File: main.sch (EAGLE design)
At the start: 45 parts, among them IC10 FGPMMOPA6H, IC2 25LC1024-I/P, IC6 MPL3115A2LGA, IC7 FXAS21000, IC8 ADXL343BCCZ, Q1 12MHz, U1 ATMEGA1284P-PU, U2 LTC3440EMSPBF

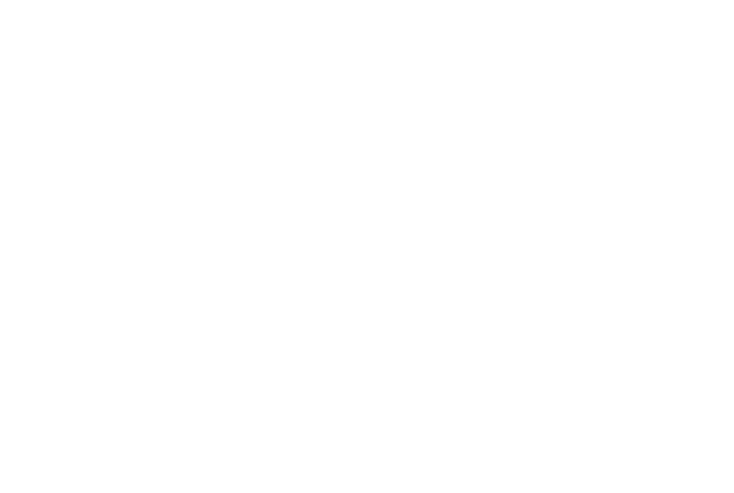
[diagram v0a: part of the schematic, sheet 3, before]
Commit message: Added datasheet for MCP9700A temperature sensor and added ambient temperature sensor to schematic.
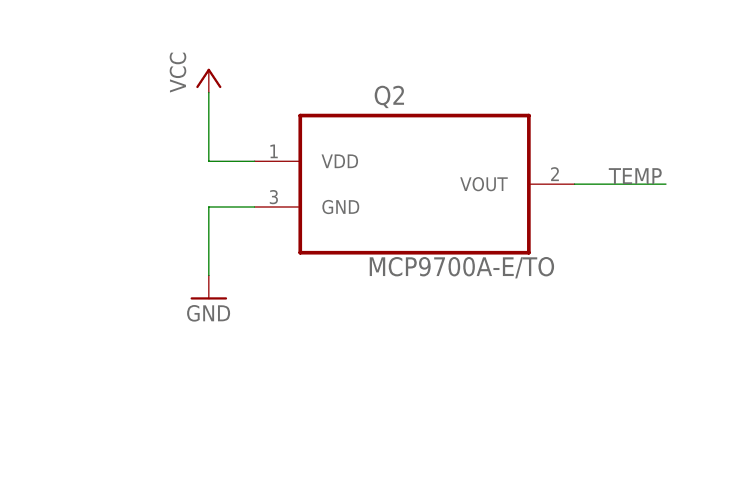
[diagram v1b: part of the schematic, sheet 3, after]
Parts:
- added Q2: MCP9700A-E/TO, CU in Space:MCP9700A-E/TO
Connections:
- removed net U2_TRIGGER: U1.PB0
- new net TEMP: Q2.VOUT, U1.PA0
- net GND: now also Q2.GND
- net VCC: now also Q2.VDD
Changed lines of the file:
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@@
 <part name="C10" library="rcl" library_urn="urn:adsk.eagle:library:334" deviceset="C-EU" device="025-025X050" package3d_urn="urn:adsk.eagle:package:23629/2" value="47pF"/>
 <part name="C11" library="rcl" library_urn="urn:adsk.eagle:library:334" deviceset="C-EU" device="025-025X050" package3d_urn="urn:adsk.eagle:package:23629/2" value="1µF"/>
+<part name="Q2" library="CU in Space" deviceset="MCP9700A-E/TO" device=""/>
+<part name="P+6" library="supply1" library_urn="urn:adsk.eagle:library:371" deviceset="VCC" device=""/>
+<part name="GND7" library="supply1" library_urn="urn:adsk.eagle:library:371" deviceset="GND" device=""/>
 </parts>
 <sheets>
@@
 </segment>
 </net>
-<net name="U2_TRIGGER" class="0">
-<segment>
-<pinref part="U1" gate="A" pin="PB0"/>
-<wire x1="45.72" y1="116.84" x2="27.94" y2="116.84" width="0.1524" layer="91"/>
-<label x="27.94" y="116.84" size="1.778" layer="95"/>
-</segment>
-</net>
 <net name="U2_RESET" class="0">
 <segment>
@@
 <wire x1="45.72" y1="111.76" x2="27.94" y2="111.76" width="0.1524" layer="91"/>
 <label x="27.94" y="111.76" size="1.778" layer="95"/>
+</segment>
+</net>
+<net name="TEMP" class="0">
+<segment>
+<pinref part="U1" gate="A" pin="PA0"/>
+<wire x1="45.72" y1="139.7" x2="38.1" y2="139.7" width="0.1524" layer="91"/>
+<label x="38.1" y="139.7" size="1.778" layer="95"/>
 </segment>
 </net>
@@
 <instance part="FRAME1" gate="G$1" x="0" y="0"/>
 <instance part="FRAME1" gate="G$2" x="147.32" y="0"/>
+<instance part="Q2" gate="A" x="210.82" y="162.56"/>
+<instance part="P+6" gate="VCC" x="187.96" y="172.72"/>
+<instance part="GND7" gate="1" x="187.96" y="147.32"/>
 </instances>
 <busses>
@@
 <junction x="78.74" y="43.18"/>
 </segment>
+<segment>
+<pinref part="Q2" gate="A" pin="GND"/>
+<pinref part="GND7" gate="1" pin="GND"/>
+<wire x1="193.04" y1="157.48" x2="187.96" y2="157.48" width="0.1524" layer="91"/>
+<wire x1="187.96" y1="157.48" x2="187.96" y2="149.86" width="0.1524" layer="91"/>
+</segment>
 </net>
 <net name="VCC" class="0">
@@
 <junction x="27.94" y="76.2"/>
 </segment>
+<segment>
+<pinref part="Q2" gate="A" pin="VDD"/>
+<pinref part="P+6" gate="VCC" pin="VCC"/>
+<wire x1="193.04" y1="162.56" x2="187.96" y2="162.56" width="0.1524" layer="91"/>
+<wire x1="187.96" y1="162.56" x2="187.96" y2="170.18" width="0.1524" layer="91"/>
+</segment>
 </net>
 <net name="SCL" class="0">
@@
 </segment>
 </net>
+<net name="TEMP" class="0">
+<segment>
+<pinref part="Q2" gate="A" pin="VOUT"/>
+<wire x1="228.6" y1="160.02" x2="238.76" y2="160.02" width="0.1524" layer="91"/>
+<label x="232.41" y="160.02" size="1.778" layer="95"/>
+</segment>
+</net>

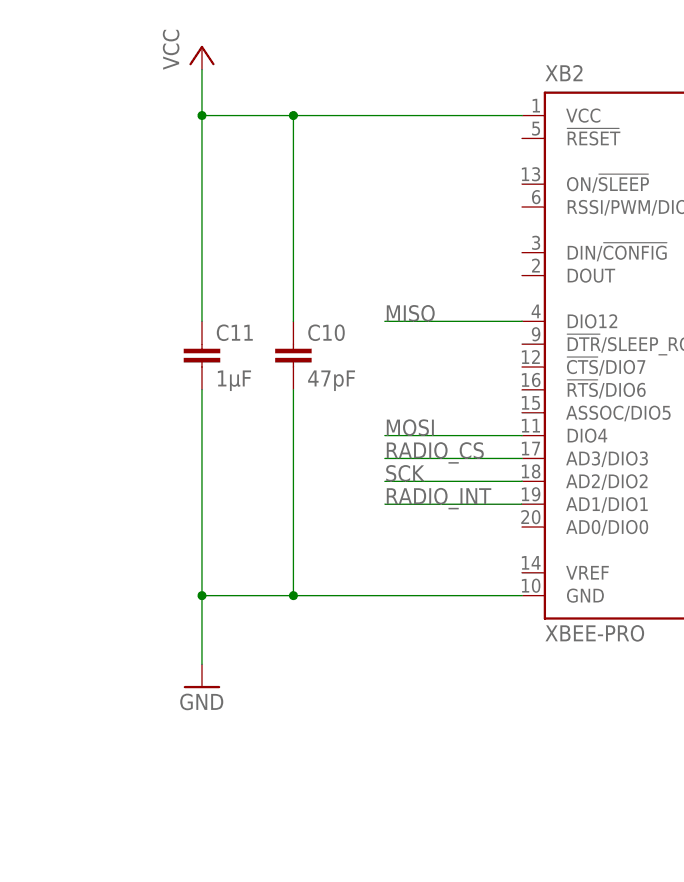
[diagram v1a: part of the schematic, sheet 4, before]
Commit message: Added high value pullups to SPI CS pins to avoid problems during programming
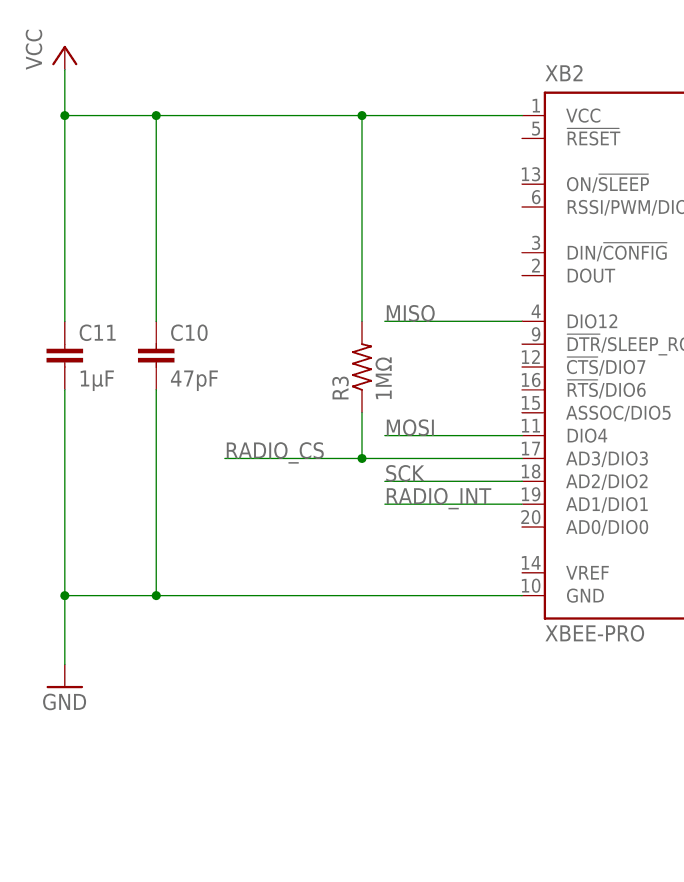
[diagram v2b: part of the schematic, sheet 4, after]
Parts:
- added R2, R3: 1MΩ, rcl:R-US_0207/5V
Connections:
- net EEPROM_CS: now also R2.1
- net RADIO_CS: now also R3.1
- net VCC: now also R2.2, R3.2
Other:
- moved on the sheet: C10, C11
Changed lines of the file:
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@@
 <part name="P+6" library="supply1" library_urn="urn:adsk.eagle:library:371" deviceset="VCC" device=""/>
 <part name="GND7" library="supply1" library_urn="urn:adsk.eagle:library:371" deviceset="GND" device=""/>
+<part name="P+7" library="supply1" library_urn="urn:adsk.eagle:library:371" deviceset="VCC" device=""/>
+<part name="R2" library="rcl" library_urn="urn:adsk.eagle:library:334" deviceset="R-US_" device="0207/5V" package3d_urn="urn:adsk.eagle:package:23502/1" value="1MΩ"/>
+<part name="R3" library="rcl" library_urn="urn:adsk.eagle:library:334" deviceset="R-US_" device="0207/5V" package3d_urn="urn:adsk.eagle:package:23502/1" value="1MΩ"/>
 </parts>
 <sheets>
@@
 <instance part="FRAME3" gate="G$1" x="0" y="-2.54"/>
 <instance part="FRAME3" gate="G$2" x="147.32" y="-2.54"/>
+<instance part="P+7" gate="VCC" x="180.34" y="129.54"/>
+<instance part="R2" gate="G$1" x="180.34" y="119.38" rot="R90"/>
 </instances>
 <busses>
@@
 <wire x1="147.32" y1="172.72" x2="147.32" y2="170.18" width="0.1524" layer="91"/>
 </segment>
+<segment>
+<pinref part="P+7" gate="VCC" pin="VCC"/>
+<pinref part="R2" gate="G$1" pin="2"/>
+<wire x1="180.34" y1="127" x2="180.34" y2="124.46" width="0.1524" layer="91"/>
+</segment>
 </net>
 <net name="XTAL1" class="0">
@@
 <segment>
 <pinref part="IC2" gate="G$1" pin="!CS"/>
-<wire x1="187.96" y1="111.76" x2="167.64" y2="111.76" width="0.1524" layer="91"/>
-<label x="167.64" y="111.76" size="1.778" layer="95"/>
+<wire x1="187.96" y1="111.76" x2="180.34" y2="111.76" width="0.1524" layer="91"/>
+<label x="162.56" y="111.76" size="1.778" layer="95"/>
+<pinref part="R2" gate="G$1" pin="1"/>
+<wire x1="180.34" y1="111.76" x2="162.56" y2="111.76" width="0.1524" layer="91"/>
+<wire x1="180.34" y1="114.3" x2="180.34" y2="111.76" width="0.1524" layer="91"/>
+<junction x="180.34" y="111.76"/>
 </segment>
 </net>
@@
 <instance part="FRAME4" gate="G$2" x="147.32" y="0"/>
 <instance part="XB2" gate="G$1" x="101.6" y="121.92"/>
-<instance part="P+5" gate="VCC" x="50.8" y="154.94"/>
-<instance part="GND6" gate="1" x="50.8" y="83.82"/>
-<instance part="C10" gate="G$1" x="60.96" y="121.92"/>
-<instance part="C11" gate="G$1" x="50.8" y="121.92"/>
+<instance part="P+5" gate="VCC" x="35.56" y="154.94"/>
+<instance part="GND6" gate="1" x="35.56" y="83.82"/>
+<instance part="C10" gate="G$1" x="45.72" y="121.92"/>
+<instance part="C11" gate="G$1" x="35.56" y="121.92"/>
+<instance part="R3" gate="G$1" x="68.58" y="119.38" rot="R90"/>
 </instances>
 <busses>
@@
 <segment>
 <pinref part="GND6" gate="1" pin="GND"/>
-<wire x1="50.8" y1="116.84" x2="50.8" y2="93.98" width="0.1524" layer="91"/>
+<wire x1="35.56" y1="116.84" x2="35.56" y2="93.98" width="0.1524" layer="91"/>
 <pinref part="XB2" gate="G$1" pin="GND"/>
-<wire x1="50.8" y1="93.98" x2="50.8" y2="86.36" width="0.1524" layer="91"/>
-<wire x1="86.36" y1="93.98" x2="60.96" y2="93.98" width="0.1524" layer="91"/>
-<junction x="50.8" y="93.98"/>
+<wire x1="35.56" y1="93.98" x2="35.56" y2="86.36" width="0.1524" layer="91"/>
+<wire x1="86.36" y1="93.98" x2="45.72" y2="93.98" width="0.1524" layer="91"/>
+<junction x="35.56" y="93.98"/>
 <pinref part="C10" gate="G$1" pin="2"/>
-<wire x1="60.96" y1="93.98" x2="50.8" y2="93.98" width="0.1524" layer="91"/>
-<wire x1="60.96" y1="116.84" x2="60.96" y2="93.98" width="0.1524" layer="91"/>
-<junction x="60.96" y="93.98"/>
+<wire x1="45.72" y1="93.98" x2="35.56" y2="93.98" width="0.1524" layer="91"/>
+<wire x1="45.72" y1="116.84" x2="45.72" y2="93.98" width="0.1524" layer="91"/>
+<junction x="45.72" y="93.98"/>
 <pinref part="C11" gate="G$1" pin="2"/>
 </segment>
@@
 <pinref part="XB2" gate="G$1" pin="VCC"/>
 <pinref part="P+5" gate="VCC" pin="VCC"/>
-<wire x1="86.36" y1="147.32" x2="60.96" y2="147.32" width="0.1524" layer="91"/>
-<wire x1="60.96" y1="147.32" x2="50.8" y2="147.32" width="0.1524" layer="91"/>
-<wire x1="50.8" y1="147.32" x2="50.8" y2="152.4" width="0.1524" layer="91"/>
-<wire x1="50.8" y1="147.32" x2="50.8" y2="124.46" width="0.1524" layer="91"/>
-<junction x="50.8" y="147.32"/>
+<wire x1="86.36" y1="147.32" x2="68.58" y2="147.32" width="0.1524" layer="91"/>
+<wire x1="68.58" y1="147.32" x2="45.72" y2="147.32" width="0.1524" layer="91"/>
+<wire x1="45.72" y1="147.32" x2="35.56" y2="147.32" width="0.1524" layer="91"/>
+<wire x1="35.56" y1="147.32" x2="35.56" y2="152.4" width="0.1524" layer="91"/>
+<wire x1="35.56" y1="147.32" x2="35.56" y2="124.46" width="0.1524" layer="91"/>
+<junction x="35.56" y="147.32"/>
 <pinref part="C10" gate="G$1" pin="1"/>
-<wire x1="60.96" y1="147.32" x2="60.96" y2="124.46" width="0.1524" layer="91"/>
-<junction x="60.96" y="147.32"/>
+<wire x1="45.72" y1="147.32" x2="45.72" y2="124.46" width="0.1524" layer="91"/>
+<junction x="45.72" y="147.32"/>
 <pinref part="C11" gate="G$1" pin="1"/>
+<pinref part="R3" gate="G$1" pin="2"/>
+<wire x1="68.58" y1="124.46" x2="68.58" y2="147.32" width="0.1524" layer="91"/>
+<junction x="68.58" y="147.32"/>
 </segment>
 </net>
@@
 <segment>
 <pinref part="XB2" gate="G$1" pin="AD3/DIO3"/>
-<wire x1="86.36" y1="109.22" x2="71.12" y2="109.22" width="0.1524" layer="91"/>
-<label x="71.12" y="109.22" size="1.778" layer="95"/>
-</segment>
-</net>
+<wire x1="86.36" y1="109.22" x2="68.58" y2="109.22" width="0.1524" layer="91"/>
+<label x="53.34" y="109.22" size="1.778" layer="95"/>
+<pinref part="R3" gate="G$1" pin="1"/>
+<wire x1="68.58" y1="109.22" x2="53.34" y2="109.22" width="0.1524" layer="91"/>
+<wire x1="68.58" y1="114.3" x2="68.58" y2="109.22" width="0.1524" layer="91"/>
+<junction x="68.58" y="109.22"/>
+</segment>
+</net>

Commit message: Voltage Regulator added
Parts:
- removed BAT1: (no value), adafruit:JST_2PIN-THM
- removed C24: 22µF, rcl:CPOL-USE2-5
- removed C25: 1.5nF, rcl:C-EU025-025X050
- removed RT1: 60.4kΩ, rcl:R-US_0207/5V
- added C12, C15: 1n, Power:K102K15X7RF5TL2
- added C13, C14: 22u, Power:UST1V220MDD
- added C16: 10n, Power:K103K15X7RF5TL2
- added C18: (no value), Power:K104K15X7RF5TL2
- added C19: (no value), Power:UST1V220MDD
- added C20: (no value), Power:FG18X7R1A225KRT06
- added D1, D2, D3: (no value), Power:SB230TA
- added L1: 18u, Power:RLB0914-180KL
- added R11: 24.9k, Power:MFR-25FBF52-24K9
- added R12: 51.1k, Power:MFR-25FBF52-51K1
- added R13: 17.4k, Power:MFR-25FBF52-17K4
- added R14: (no value), Power:MFR-25FBF52-51K1
- added R15: (no value), Power:MFR-25FBF52-26K7
- added R7: 8.06k, Power:MFR-25FBF52-8K06
- added U3: 2N3904BU, Power:2N3904BU
- C7: value 10µF -> 10n; device rcl:CPOL-USE2-5 -> Power:K103K15X7RF5TL2
- L3: value 10µH -> (none); device rcl:L-US0207/5V -> Power:B78108E1472K000
- R10: value 15kΩ -> 24.9k; device rcl:R-US_0207/5V -> Power:MFR-25FBF52-24K9
- R8: value 340kΩ -> 51.1k; device rcl:R-US_0207/5V -> Power:MFR-25FBF52-51K1
- R9: value 200kΩ -> 3.65k; device rcl:R-US_0207/5V -> Power:MFR-25FBF52-3K65
- U2: value LTC3440EMSPBF -> LT3570EFEPBF; device CU in Space:LTC3440EMSPBF -> Power:LT3570EFEPBF
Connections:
- removed net FB: R10.1, R8.1, R9.2, U2.FB
- removed net N$14: C25.1, U2.VC
- removed net VBAT1: BAT1.2, C7.+, U2.VIN, U2.~SHDN/SS
- new net +12.0: C14.+, D1.C, R8.11
- new net +2.5: C20.1, R14.11, U3.E
- new net FB1: R8.22, R9.11, U2.FB1
- new net N$15: R12.11, R13.22, U2.FB2
- new net N$16: C18.1, D3.C, U2.BOOST
- new net N$17: R14.22, R15.11, U2.FB3
- new net N$5: C7.1, U2.SS2
- new net N$6: R7.22, U2.RT
- new net N$7: R10.22, U2.VC2
- new net N$8: D1.A, L1.2, U2.SW1
- new net N$9: C15.1, R11.22
- new net NPN_DRV: U2.NPN_DRV, U3.B
- new net PWR_JUNC: C13.+, L1.1, U2.!SHDN1, U2.!SHDN2, U2.!SHDN3, U2.VIN1, U2.VIN2, U2.VIN3
- net GND: now also C12.2, C13.-, C14.-, C15.2, C16.2, C19.-, C20.2, C7.2, D2.A, R13.11, R15.22, R7.11, R9.22, U2.GND, U2.SYNC; no longer BAT1.1, C24.-, C7.-, R9.1, RT1.1, U2.MODE/SYNC
- net N$10: now also C12.1, R10.11; no longer L3.1, U2.SW1
- net N$11: now also R11.11, U2.VC1; no longer L3.2, U2.SW2
- net N$12: now also C16.1, U2.SS1; no longer RT1.2, U2.RT
- net N$13: now also C18.2, D2.C, L3.1, U2.SW2; no longer C25.2, R10.2
- net VCC: now also C19.+, D3.A, L3.2, R12.22, U3.C; no longer C24.+, R8.2, U2.VOUT
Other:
- note added: "Colin Andersen Nov 13 2017"
- note added: "NET CLASSES (NET NAME = VOLTAGE) +2.5 = 2.5V +VCC = 3.3V +5.0 = 5.0V +12.0 = 12.0V"
- note added: "Power - Regulator"
- note removed: "Power"

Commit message: Mostly routed
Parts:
- removed C18: (no value), Power:K104K15X7RF5TL2
- added DC1: PJ-102BH, Power:PJ-102BH
- added Q3: FQP7P06, Power:FQP7P06
- added R16: 51.1kΩ, Power:MFR-25FBF52-51K1
- added XLR1: NC3FAH1, Power:NC3FAH1
- added XLR2: NC5FAH, Power:NC5FAH
- C1, C27, C28: value 100nF -> 0.1µF
- C12, C15: value 1n -> 1nF
- C13, C14: value 22u -> 22µF
- C16, C7: value 10n -> 10nF
- C19: value (none) -> 22µF
- C20: value (none) -> 0.1µF; device Power:FG18X7R1A225KRT06 -> rcl:C-EU025-025X050
- L1: value 18u -> 18µH
- L3: value (none) -> 4.7µH
- R10, R11: value 24.9k -> 24.9kΩ
- R12, R8: value 51.1k -> 51.1kΩ
- R13: value 17.4k -> 17.4kΩ
- R14: value (none) -> 3.65kΩ; device Power:MFR-25FBF52-51K1 -> Power:MFR-25FBF52-3K65
- R15: value (none) -> 51.1kΩ; device Power:MFR-25FBF52-26K7 -> Power:MFR-25FBF52-51K1
- R7: value 8.06k -> 8.06kΩ
- R9: value 3.65k -> 3.65kΩ
- U3: value 2N3904BU -> TL431BQLP; device Power:2N3904BU -> Power:TL431BQLP
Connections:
- removed net +2.5: C20.1, R14.11, U3.E
- removed net N$17: R14.22, R15.11, U2.FB3
- removed net NPN_DRV: U2.NPN_DRV, U3.B
- new net BAT+: Q3.S, R14.11, R15.11, XLR1.OUT1
- new net N$30: DC1.SW, XLR1.GND, XLR1.OUT2
- new net N$69: Q3.G, R14.22, U3.CATHODE
- new net N$70: R15.22, R16.11, U3.REF
- net GND: now also DC1.GND, R16.22, U2.!SHDN3, U2.EPAD, U3.ANODE, XLR2.GND; no longer C20.2, R15.22
- net N$13: now also C20.2; no longer C18.2
- net N$16: now also C20.1; no longer C18.1
- net PWR_JUNC: now also DC1.+12V, Q3.D; no longer U2.!SHDN3, U2.VIN3
- net VCC: no longer U3.C
